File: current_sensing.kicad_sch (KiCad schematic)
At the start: 6 parts, among them U10 INA181A1

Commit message: started silkscrean
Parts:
- renumbered C32 to C35, C33 to C36, C34 to C37, R68 to R69, R69 to R70, U10 to U7
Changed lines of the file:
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@@
 		(on_board yes)
 		(dnp no)
-		(property "Reference" "U10"
+		(property "Reference" "U7"
 			(at 124.206 82.55 0)
 			(effects
@@
 			(project "frodo_io_module"
 				(path "/c1ccca3c-4648-4b8e-86a1-690c24c5f13e/0381ad7c-a4fe-46cf-80e9-20458dbb02ae"
-					(reference "U11")
-					(unit 1)
-				)
-				(path "/c1ccca3c-4648-4b8e-86a1-690c24c5f13e/503665e4-7dbc-4cb7-9fc2-35263499a935"
-					(reference "U1")
-					(unit 1)
-				)
-				(path "/c1ccca3c-4648-4b8e-86a1-690c24c5f13e/b9f805af-f42c-49d8-9c2b-cbc55b6b7bfe"
-					(reference "U10")
+					(reference "U8")
+					(unit 1)
+				)
+				(path "/c1ccca3c-4648-4b8e-86a1-690c24c5f13e/503665e4-7dbc-4cb7-9fc2-35263499a935"
+					(reference "U9")
+					(unit 1)
+				)
+				(path "/c1ccca3c-4648-4b8e-86a1-690c24c5f13e/b9f805af-f42c-49d8-9c2b-cbc55b6b7bfe"
+					(reference "U7")
 					(unit 1)
 				)
@@
 		(on_board yes)
 		(dnp no)
-		(property "Reference" "C32"
+		(property "Reference" "C35"
 			(at 129.794 71.882 90)
 			(effects
@@
 			(project "frodo_io_module"
 				(path "/c1ccca3c-4648-4b8e-86a1-690c24c5f13e/0381ad7c-a4fe-46cf-80e9-20458dbb02ae"
+					(reference "C38")
+					(unit 1)
+				)
+				(path "/c1ccca3c-4648-4b8e-86a1-690c24c5f13e/503665e4-7dbc-4cb7-9fc2-35263499a935"
+					(reference "C41")
+					(unit 1)
+				)
+				(path "/c1ccca3c-4648-4b8e-86a1-690c24c5f13e/b9f805af-f42c-49d8-9c2b-cbc55b6b7bfe"
 					(reference "C35")
-					(unit 1)
-				)
-				(path "/c1ccca3c-4648-4b8e-86a1-690c24c5f13e/503665e4-7dbc-4cb7-9fc2-35263499a935"
-					(reference "C38")
-					(unit 1)
-				)
-				(path "/c1ccca3c-4648-4b8e-86a1-690c24c5f13e/b9f805af-f42c-49d8-9c2b-cbc55b6b7bfe"
-					(reference "C32")
 					(unit 1)
 				)
@@
 		(on_board yes)
 		(dnp no)
-		(property "Reference" "R69"
+		(property "Reference" "R70"
 			(at 101.6 89.662 90)
 			(effects
@@
 			(project "frodo_io_module"
 				(path "/c1ccca3c-4648-4b8e-86a1-690c24c5f13e/0381ad7c-a4fe-46cf-80e9-20458dbb02ae"
-					(reference "R71")
-					(unit 1)
-				)
-				(path "/c1ccca3c-4648-4b8e-86a1-690c24c5f13e/503665e4-7dbc-4cb7-9fc2-35263499a935"
-					(reference "R16")
-					(unit 1)
-				)
-				(path "/c1ccca3c-4648-4b8e-86a1-690c24c5f13e/b9f805af-f42c-49d8-9c2b-cbc55b6b7bfe"
-					(reference "R69")
+					(reference "R72")
+					(unit 1)
+				)
+				(path "/c1ccca3c-4648-4b8e-86a1-690c24c5f13e/503665e4-7dbc-4cb7-9fc2-35263499a935"
+					(reference "R74")
+					(unit 1)
+				)
+				(path "/c1ccca3c-4648-4b8e-86a1-690c24c5f13e/b9f805af-f42c-49d8-9c2b-cbc55b6b7bfe"
+					(reference "R70")
 					(unit 1)
 				)
@@
 				)
 				(path "/c1ccca3c-4648-4b8e-86a1-690c24c5f13e/503665e4-7dbc-4cb7-9fc2-35263499a935"
-					(reference "#FLG05")
+					(reference "#FLG010")
 					(unit 1)
 				)
@@
 		(dnp no)
 		(fields_autoplaced yes)
-		(property "Reference" "#PWR0135"
+		(property "Reference" "#PWR0122"
 			(at 138.43 85.09 0)
 			(effects
@@
 			(project "frodo_io_module"
 				(path "/c1ccca3c-4648-4b8e-86a1-690c24c5f13e/0381ad7c-a4fe-46cf-80e9-20458dbb02ae"
-					(reference "#PWR0140")
-					(unit 1)
-				)
-				(path "/c1ccca3c-4648-4b8e-86a1-690c24c5f13e/503665e4-7dbc-4cb7-9fc2-35263499a935"
-					(reference "#PWR017")
-					(unit 1)
-				)
-				(path "/c1ccca3c-4648-4b8e-86a1-690c24c5f13e/b9f805af-f42c-49d8-9c2b-cbc55b6b7bfe"
-					(reference "#PWR0135")
+					(reference "#PWR0127")
+					(unit 1)
+				)
+				(path "/c1ccca3c-4648-4b8e-86a1-690c24c5f13e/503665e4-7dbc-4cb7-9fc2-35263499a935"
+					(reference "#PWR0132")
+					(unit 1)
+				)
+				(path "/c1ccca3c-4648-4b8e-86a1-690c24c5f13e/b9f805af-f42c-49d8-9c2b-cbc55b6b7bfe"
+					(reference "#PWR0122")
 					(unit 1)
 				)
@@
 		(on_board yes)
 		(dnp no)
-		(property "Reference" "#PWR0134"
+		(property "Reference" "#PWR0121"
 			(at 119.38 80.01 0)
 			(effects
@@
 			(project "frodo_io_module"
 				(path "/c1ccca3c-4648-4b8e-86a1-690c24c5f13e/0381ad7c-a4fe-46cf-80e9-20458dbb02ae"
-					(reference "#PWR0139")
-					(unit 1)
-				)
-				(path "/c1ccca3c-4648-4b8e-86a1-690c24c5f13e/503665e4-7dbc-4cb7-9fc2-35263499a935"
-					(reference "#PWR016")
-					(unit 1)
-				)
-				(path "/c1ccca3c-4648-4b8e-86a1-690c24c5f13e/b9f805af-f42c-49d8-9c2b-cbc55b6b7bfe"
-					(reference "#PWR0134")
+					(reference "#PWR0126")
+					(unit 1)
+				)
+				(path "/c1ccca3c-4648-4b8e-86a1-690c24c5f13e/503665e4-7dbc-4cb7-9fc2-35263499a935"
+					(reference "#PWR0131")
+					(unit 1)
+				)
+				(path "/c1ccca3c-4648-4b8e-86a1-690c24c5f13e/b9f805af-f42c-49d8-9c2b-cbc55b6b7bfe"
+					(reference "#PWR0121")
 					(unit 1)
 				)
@@
 		(on_board yes)
 		(dnp no)
-		(property "Reference" "R68"
+		(property "Reference" "R69"
 			(at 101.6 84.582 90)
 			(effects
@@
 			(project "frodo_io_module"
 				(path "/c1ccca3c-4648-4b8e-86a1-690c24c5f13e/0381ad7c-a4fe-46cf-80e9-20458dbb02ae"
-					(reference "R70")
-					(unit 1)
-				)
-				(path "/c1ccca3c-4648-4b8e-86a1-690c24c5f13e/503665e4-7dbc-4cb7-9fc2-35263499a935"
-					(reference "R15")
-					(unit 1)
-				)
-				(path "/c1ccca3c-4648-4b8e-86a1-690c24c5f13e/b9f805af-f42c-49d8-9c2b-cbc55b6b7bfe"
-					(reference "R68")
+					(reference "R71")
+					(unit 1)
+				)
+				(path "/c1ccca3c-4648-4b8e-86a1-690c24c5f13e/503665e4-7dbc-4cb7-9fc2-35263499a935"
+					(reference "R73")
+					(unit 1)
+				)
+				(path "/c1ccca3c-4648-4b8e-86a1-690c24c5f13e/b9f805af-f42c-49d8-9c2b-cbc55b6b7bfe"
+					(reference "R69")
 					(unit 1)
 				)
@@
 		(on_board yes)
 		(dnp no)
-		(property "Reference" "C33"
+		(property "Reference" "C36"
 			(at 99.06 96.52 0)
 			(effects
@@
 			(project "frodo_io_module"
 				(path "/c1ccca3c-4648-4b8e-86a1-690c24c5f13e/0381ad7c-a4fe-46cf-80e9-20458dbb02ae"
+					(reference "C39")
+					(unit 1)
+				)
+				(path "/c1ccca3c-4648-4b8e-86a1-690c24c5f13e/503665e4-7dbc-4cb7-9fc2-35263499a935"
+					(reference "C42")
+					(unit 1)
+				)
+				(path "/c1ccca3c-4648-4b8e-86a1-690c24c5f13e/b9f805af-f42c-49d8-9c2b-cbc55b6b7bfe"
 					(reference "C36")
-					(unit 1)
-				)
-				(path "/c1ccca3c-4648-4b8e-86a1-690c24c5f13e/503665e4-7dbc-4cb7-9fc2-35263499a935"
-					(reference "C40")
-					(unit 1)
-				)
-				(path "/c1ccca3c-4648-4b8e-86a1-690c24c5f13e/b9f805af-f42c-49d8-9c2b-cbc55b6b7bfe"
-					(reference "C33")
 					(unit 1)
 				)
@@
 		(on_board yes)
 		(dnp no)
-		(property "Reference" "C34"
+		(property "Reference" "C37"
 			(at 113.03 96.52 0)
 			(effects
@@
 			(project "frodo_io_module"
 				(path "/c1ccca3c-4648-4b8e-86a1-690c24c5f13e/0381ad7c-a4fe-46cf-80e9-20458dbb02ae"
+					(reference "C40")
+					(unit 1)
+				)
+				(path "/c1ccca3c-4648-4b8e-86a1-690c24c5f13e/503665e4-7dbc-4cb7-9fc2-35263499a935"
+					(reference "C43")
+					(unit 1)
+				)
+				(path "/c1ccca3c-4648-4b8e-86a1-690c24c5f13e/b9f805af-f42c-49d8-9c2b-cbc55b6b7bfe"
 					(reference "C37")
-					(unit 1)
-				)
-				(path "/c1ccca3c-4648-4b8e-86a1-690c24c5f13e/503665e4-7dbc-4cb7-9fc2-35263499a935"
-					(reference "C41")
-					(unit 1)
-				)
-				(path "/c1ccca3c-4648-4b8e-86a1-690c24c5f13e/b9f805af-f42c-49d8-9c2b-cbc55b6b7bfe"
-					(reference "C34")
 					(unit 1)
 				)
@@
 		(dnp no)
 		(fields_autoplaced yes)
-		(property "Reference" "#PWR0136"
+		(property "Reference" "#PWR0123"
 			(at 119.38 102.87 0)
 			(effects
@@
 			(project "frodo_io_module"
 				(path "/c1ccca3c-4648-4b8e-86a1-690c24c5f13e/0381ad7c-a4fe-46cf-80e9-20458dbb02ae"
-					(reference "#PWR0141")
-					(unit 1)
-				)
-				(path "/c1ccca3c-4648-4b8e-86a1-690c24c5f13e/503665e4-7dbc-4cb7-9fc2-35263499a935"
-					(reference "#PWR019")
-					(unit 1)
-				)
-				(path "/c1ccca3c-4648-4b8e-86a1-690c24c5f13e/b9f805af-f42c-49d8-9c2b-cbc55b6b7bfe"
-					(reference "#PWR0136")
+					(reference "#PWR0128")
+					(unit 1)
+				)
+				(path "/c1ccca3c-4648-4b8e-86a1-690c24c5f13e/503665e4-7dbc-4cb7-9fc2-35263499a935"
+					(reference "#PWR0133")
+					(unit 1)
+				)
+				(path "/c1ccca3c-4648-4b8e-86a1-690c24c5f13e/b9f805af-f42c-49d8-9c2b-cbc55b6b7bfe"
+					(reference "#PWR0123")
 					(unit 1)
 				)
@@
 		(dnp no)
 		(fields_autoplaced yes)
-		(property "Reference" "#PWR0138"
+		(property "Reference" "#PWR0125"
 			(at 110.49 107.95 0)
 			(effects
@@
 			(project "frodo_io_module"
 				(path "/c1ccca3c-4648-4b8e-86a1-690c24c5f13e/0381ad7c-a4fe-46cf-80e9-20458dbb02ae"
-					(reference "#PWR0143")
-					(unit 1)
-				)
-				(path "/c1ccca3c-4648-4b8e-86a1-690c24c5f13e/503665e4-7dbc-4cb7-9fc2-35263499a935"
-					(reference "#PWR034")
-					(unit 1)
-				)
-				(path "/c1ccca3c-4648-4b8e-86a1-690c24c5f13e/b9f805af-f42c-49d8-9c2b-cbc55b6b7bfe"
-					(reference "#PWR0138")
+					(reference "#PWR0130")
+					(unit 1)
+				)
+				(path "/c1ccca3c-4648-4b8e-86a1-690c24c5f13e/503665e4-7dbc-4cb7-9fc2-35263499a935"
+					(reference "#PWR0135")
+					(unit 1)
+				)
+				(path "/c1ccca3c-4648-4b8e-86a1-690c24c5f13e/b9f805af-f42c-49d8-9c2b-cbc55b6b7bfe"
+					(reference "#PWR0125")
 					(unit 1)
 				)
@@
 		(dnp no)
 		(fields_autoplaced yes)
-		(property "Reference" "#PWR0137"
+		(property "Reference" "#PWR0124"
 			(at 105.41 107.95 0)
 			(effects
@@
 			(project "frodo_io_module"
 				(path "/c1ccca3c-4648-4b8e-86a1-690c24c5f13e/0381ad7c-a4fe-46cf-80e9-20458dbb02ae"
-					(reference "#PWR0142")
-					(unit 1)
-				)
-				(path "/c1ccca3c-4648-4b8e-86a1-690c24c5f13e/503665e4-7dbc-4cb7-9fc2-35263499a935"
-					(reference "#PWR023")
-					(unit 1)
-				)
-				(path "/c1ccca3c-4648-4b8e-86a1-690c24c5f13e/b9f805af-f42c-49d8-9c2b-cbc55b6b7bfe"
-					(reference "#PWR0137")
-					(unit 1)
-				)
+					(reference "#PWR0129")
+					(unit 1)
+				)
+				(path "/c1ccca3c-4648-4b8e-86a1-690c24c5f13e/503665e4-7dbc-4cb7-9fc2-35263499a935"
+					(reference "#PWR0134")
+					(unit 1)
+				)
+				(path "/c1ccca3c-4648-4b8e-86a1-690c24c5f13e/b9f805af-f42c-49d8-9c2b-cbc55b6b7bfe"
+					(reference "#PWR0124")
+					(unit 1)
+				)

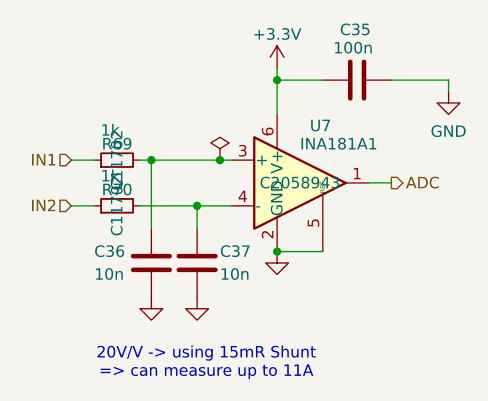
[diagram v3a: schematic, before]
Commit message: silkscreen improvements, change mosfets, fix diode footprint
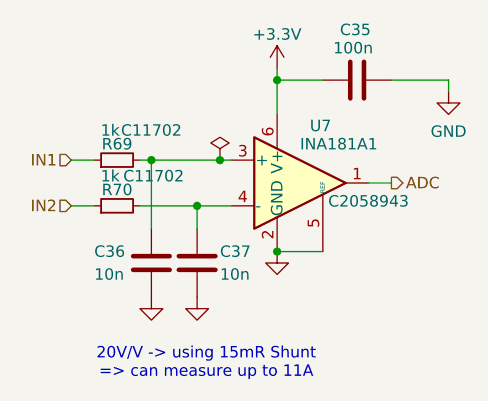
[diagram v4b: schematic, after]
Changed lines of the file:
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@@
 		)
 		(property "LCSC" "C2058943"
-			(at 121.92 88.9 0)
+			(at 129.54 90.932 0)
 			(show_name no)
 			(do_not_autoplace no)
@@
 		)
 		(property "LCSC" "C11702"
-			(at 101.6 91.44 0)
+			(at 105.664 88.138 90)
 			(show_name no)
 			(do_not_autoplace no)
@@
 		)
 		(property "LCSC" "C11702"
-			(at 101.6 86.36 0)
-			(show_name no)
-			(do_not_autoplace no)
+			(at 105.41 83.058 90)
+			(show_name no)
+			(do_not_autoplace no)

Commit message: some last adaptaions while ordering
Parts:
- C35: LCSC# C77020 -> C1525
- U7: LCSC C2058943 -> C45351496
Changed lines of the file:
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@@
 			)
 		)
-		(property "LCSC" "C2058943"
+		(property "LCSC" "C45351496"
 			(at 129.54 90.932 0)
 			(show_name no)
@@
 			)
 		)
-		(property "LCSC#" "C77020"
+		(property "LCSC#" " C1525"
 			(at 128.27 77.47 0)
 			(hide yes)
